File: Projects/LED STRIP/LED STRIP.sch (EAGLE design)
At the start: 70 parts, among them U1 PCA9635, U2 PCA9635, U3 PCA9635

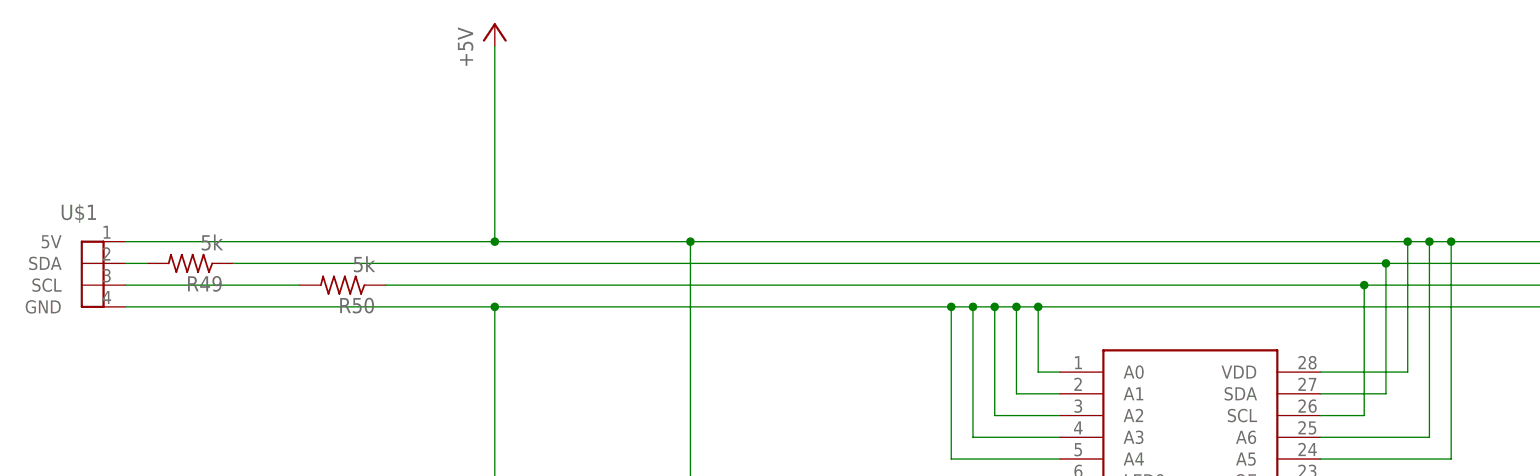
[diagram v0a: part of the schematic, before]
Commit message: moved SCL and SDA resistors to proper location
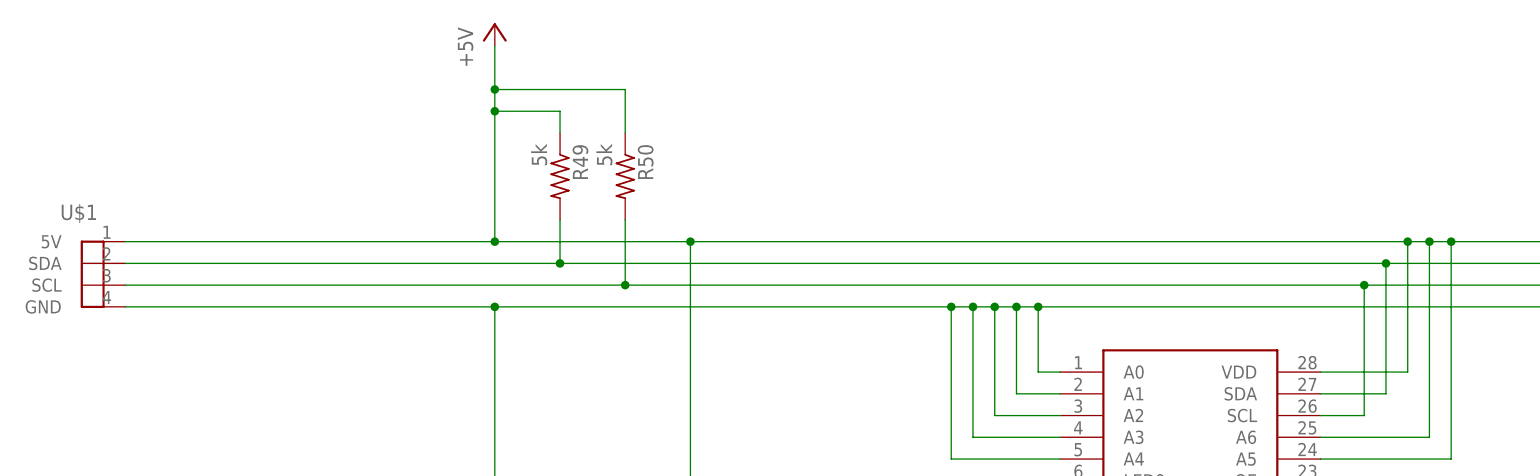
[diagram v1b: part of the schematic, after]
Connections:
- removed net N$1: R49.1, U1.SDA, U2.SDA, U3.SDA
- removed net N$2: R50.1, U1.SCL, U2.SCL, U3.SCL
- net +5V: now also R49.1, R50.1
- net N$51: now also U1.SDA, U2.SDA, U3.SDA
- net N$52: now also U1.SCL, U2.SCL, U3.SCL
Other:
- moved on the sheet: R49, R50

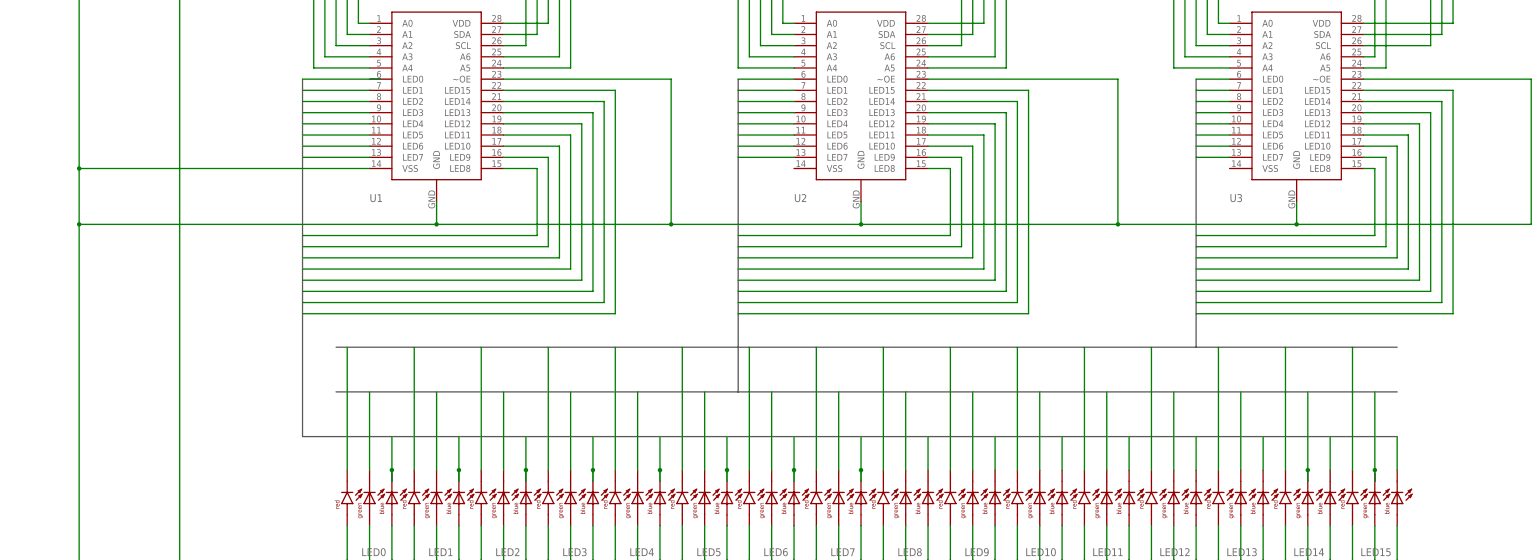
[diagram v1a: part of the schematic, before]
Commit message: updated board and schematic
-changed PCA9635 library part. removed exposed pad and copied TSSOP28
land pattern from another library
-started routing some of the traces. decided on 4 layers
-drill size of vias and trace width is not set in stone
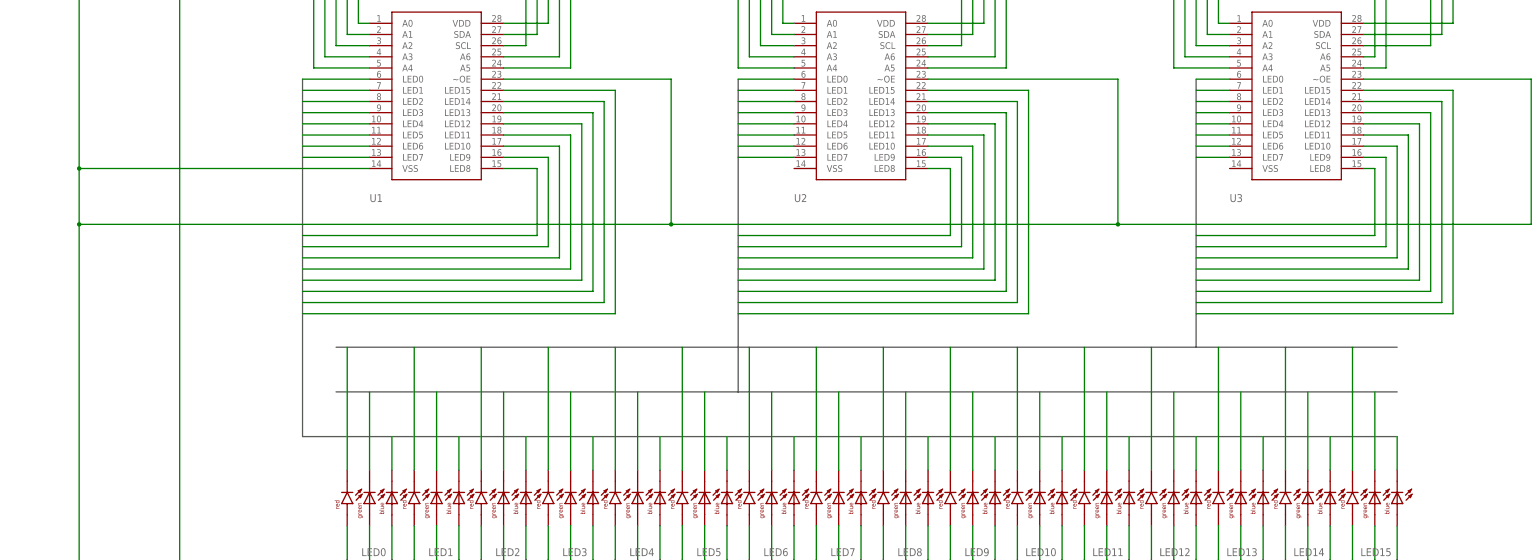
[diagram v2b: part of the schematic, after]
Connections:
- removed net BA1: U1.LED1
- removed net BA2: U1.LED2
- removed net BA3: U1.LED3
- removed net BA4: U1.LED4
- removed net BA5: U1.LED5
- removed net BA6: U1.LED6
- removed net BA7: U1.LED7
- net B0: now also U1.LED0
- net B1: now also U1.LED1
- net B2: now also U1.LED2
- net B3: now also U1.LED3
- net B4: now also U1.LED4
- net B5: now also U1.LED5
- net B6: now also U1.LED6
- net B7: now also U1.LED7
- net GND: no longer U1.GND, U2.GND, U3.GND

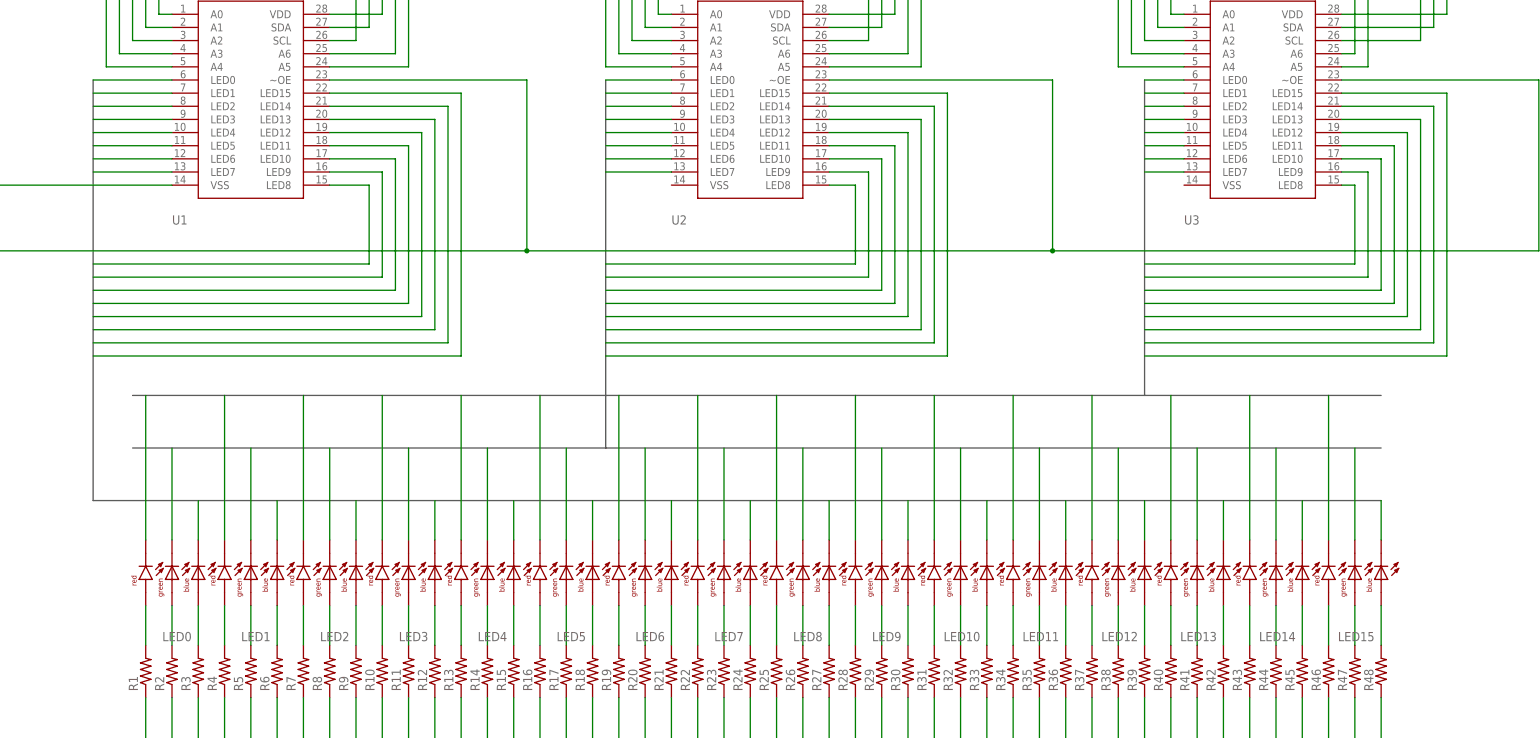
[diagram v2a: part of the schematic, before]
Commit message: changed order of LEDs to make it more routable
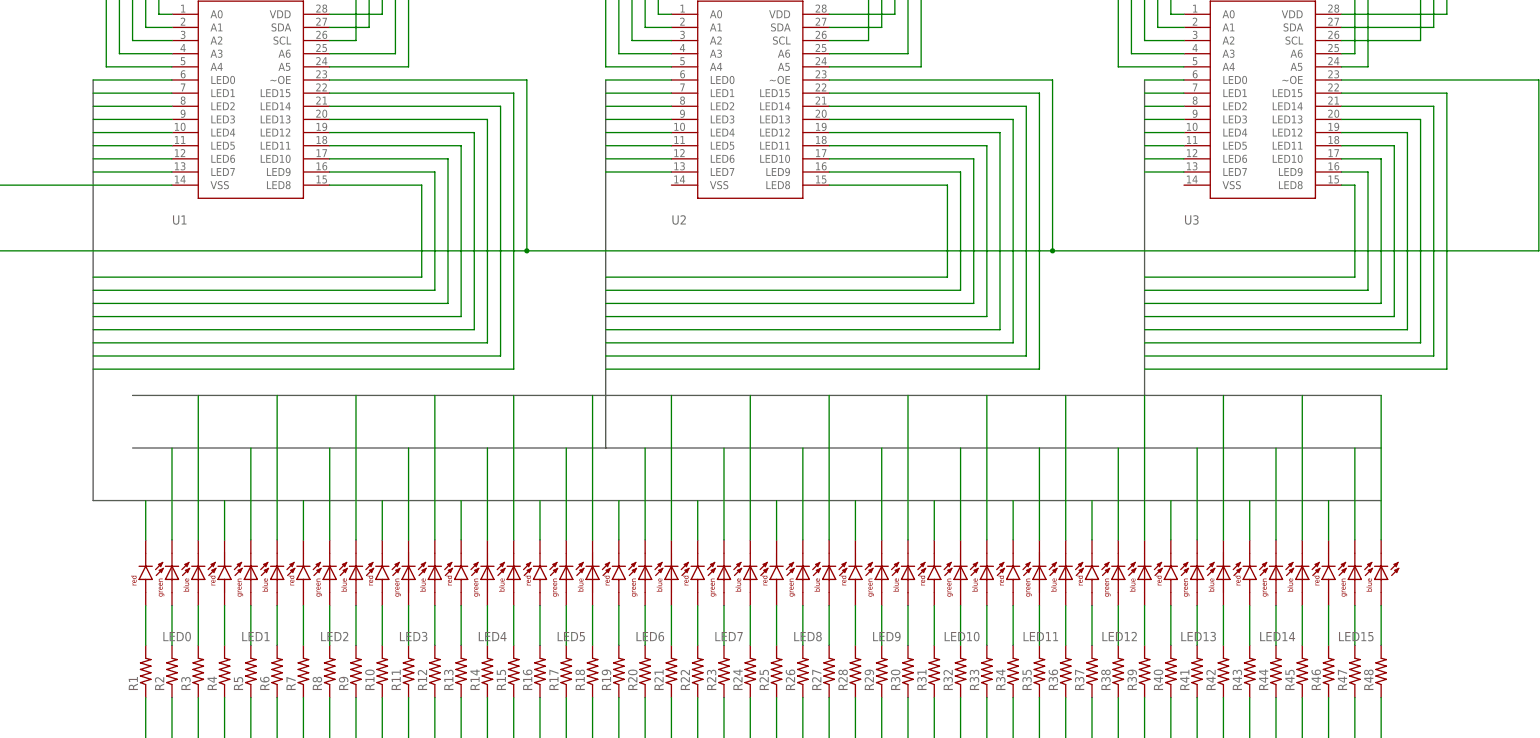
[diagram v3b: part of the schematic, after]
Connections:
- net B0 renamed RED0
- net B1 renamed RED1
- net B10 renamed RED10
- net B11 renamed RED11
- net B12 renamed RED12
- net B13 renamed RED13
- net B14 renamed RED14
- net B15 renamed RED15
- net B2 renamed RED2
- net B3 renamed RED3
- net B4 renamed RED4
- net B5 renamed RED5
- net B6 renamed RED6
- net B7 renamed RED7
- net B8 renamed RED8
- net B9 renamed RED9
- net G0 renamed GREEN0
- net G1 renamed GREEN1
- net G10 renamed GREEN10
- net G11 renamed GREEN11
- net G12 renamed GREEN12
- net G13 renamed GREEN13
- net G14 renamed GREEN14
- net G15 renamed GREEN15
- net G2 renamed GREEN2
- net G3 renamed GREEN3
- net G4 renamed GREEN4
- net G5 renamed GREEN5
- net G6 renamed GREEN6
- net G7 renamed GREEN7
- net G8 renamed GREEN8
- net G9 renamed GREEN9
- net R0 renamed BLUE0
- net R1 renamed BLUE1
- net R10 renamed BLUE10
- net R11 renamed BLUE11
- net R12 renamed BLUE12
- net R13 renamed BLUE13
- net R14 renamed BLUE14
- net R15 renamed BLUE15
- net R2 renamed BLUE2
- net R3 renamed BLUE3
- net R4 renamed BLUE4
- net R5 renamed BLUE5
- net R6 renamed BLUE6
- net R7 renamed BLUE7
- net R8 renamed BLUE8
- net R9 renamed BLUE9
- net N$11: now also LED13.4, R40.2; no longer LED2.4, R9.2
- net N$12: now also LED12.6, R39.2; no longer LED3.6, R10.2
- net N$14: now also LED10.4, R31.2; no longer LED3.4, R12.2
- net N$15: now also LED9.6, R30.2; no longer LED4.6, R13.2
- net N$17: now also LED9.4, R28.2; no longer LED4.4, R15.2
- net N$18: now also LED8.6, R27.2; no longer LED5.6, R16.2
- net N$20: now also LED7.6, R24.2; no longer LED5.4, R18.2
- net N$21: now also LED8.4, R25.2; no longer LED6.6, R19.2
- net N$23: now also LED7.4, R22.2; no longer LED6.4, R21.2
- net N$24: now also LED6.6, R21.2; no longer LED7.6, R22.2
- net N$26: now also LED6.4, R19.2; no longer LED7.4, R24.2
- net N$27: now also LED5.4, R16.2; no longer LED8.6, R25.2
- net N$29: now also LED4.6, R15.2; no longer LED8.4, R27.2
- net N$3: now also LED15.6, R48.2; no longer LED0.6, R1.2
- net N$30: now also LED4.4, R13.2; no longer LED9.6, R28.2
- net N$32: now also LED3.6, R12.2; no longer LED9.4, R30.2
- net N$33: now also LED3.4, R10.2; no longer LED10.6, R31.2
- net N$35: now also LED2.6, R9.2; no longer LED10.4, R33.2
- net N$36: now also LED1.6, R6.2; no longer LED11.6, R34.2
- net N$38: now also LED1.4, R4.2; no longer LED11.4, R36.2
- net N$39: now also LED0.6, R3.2; no longer LED12.6, R37.2
- net N$41: now also LED0.4, R1.2; no longer LED12.4, R39.2
- net N$42: now also LED2.4, R7.2; no longer LED13.6, R40.2
- net N$44: now also LED5.6, R18.2; no longer LED13.4, R42.2
- net N$45: now also LED10.6, R33.2; no longer LED14.6, R43.2
- net N$47: now also LED11.4, R34.2; no longer LED14.4, R45.2
- net N$48: now also LED11.6, R36.2; no longer LED15.6, R46.2
- net N$5: now also LED15.4, R46.2; no longer LED0.4, R3.2
- net N$50: now also LED12.4, R37.2; no longer LED15.4, R48.2
- net N$6: now also LED14.6, R45.2; no longer LED1.6, R4.2
- net N$8: now also LED14.4, R43.2; no longer LED1.4, R6.2
- net N$9: now also LED13.6, R42.2; no longer LED2.6, R7.2
